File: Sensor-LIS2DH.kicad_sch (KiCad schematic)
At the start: 4 parts, among them U5 LIS2DH

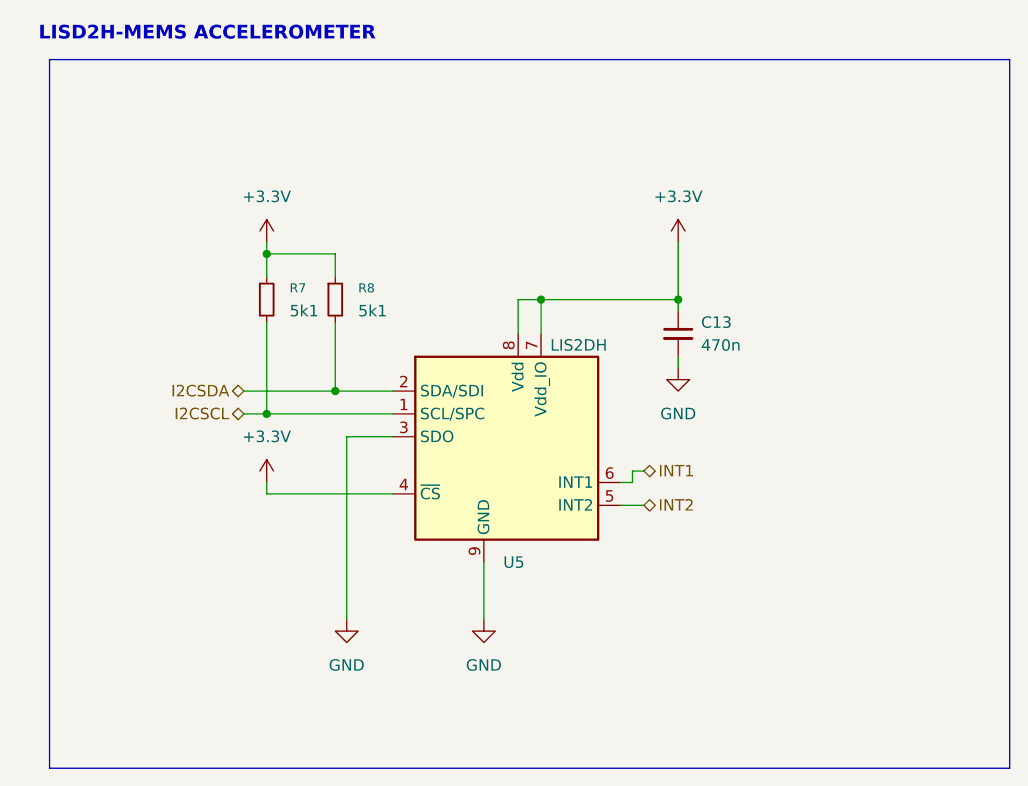
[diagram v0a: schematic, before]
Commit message: fix(hardware): update LIS2DH sensor schematic with corrected routing and metadata
- Adjust wire routing for INT1 signal path on Sensor-LIS2DH schematic
- Update datasheet URL to STMicroelectronics lis2dh12.pdf
- Add manufacturer, supplier, and part number metadata to component
- Add KLC compliance properties (KLC_S3.3, KLC_S4.1) to symbol and footprint entries
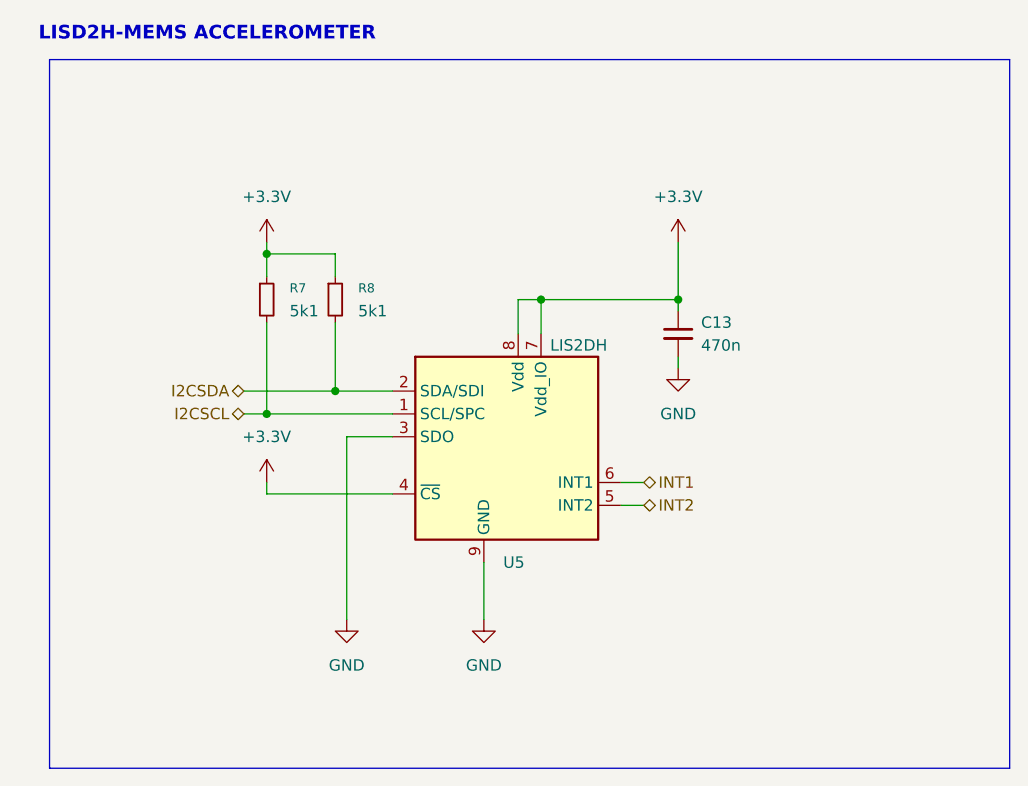
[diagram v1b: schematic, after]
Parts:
- U5: Distributor Link 1 (none) -> https://eu.mouser.com/ProductDetail/STMicroelectronics/LIS2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; Distributor Link 2  (none) -> https://www.digikey.com/en/products/detail/stmicroelectroni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; LCSC (none) -> C110926; Manufacturer (none) -> STMicroelectronics; Manufacturer part Number (none) -> LIS2DH12TR
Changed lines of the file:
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@@
-	(wire
-		(pts
-			(xy 88.9 76.2) (xy 88.9 77.47)
-		)
-		(stroke
-			(width 0)
-			(type default)
-		)
-	)
 	(wire
 		(pts
@@
 	(wire
 		(pts
-			(xy 88.9 77.47) (xy 87.63 77.47)
+			(xy 87.63 77.47) (xy 90.17 77.47)
 		)
 		(stroke
@@
 		(pts
 			(xy 48.26 77.47) (xy 48.26 78.74)
-		)
-		(stroke
-			(width 0)
-			(type default)
-		)
-	)
-	(wire
-		(pts
-			(xy 90.17 76.2) (xy 88.9 76.2)
 		)
 		(stroke
@@
 	(hierarchical_label "INT1"
 		(shape tri_state)
-		(at 90.17 76.2 0)
+		(at 90.17 77.47 0)
 		(effects
 			(font
@@
 			)
 		)
-		(property "Datasheet" "http://www.st.com/web/en/resource/technical/document/datasheet/DM00042751.pdf"
+		(property "Datasheet" "https://www.st.com/resource/en/datasheet/lis2dh12.pdf"
 			(at 72.39 88.9 0)
 			(effects
@@
 			)
 		)
-		(property "Description" "3-Axis Accelerometer, 2/4/8/16g range, I2C/SPI interface, LGA-14"
+		(property "Description" "Accelerometers MEMS digital output motion sensor: ultra-low-power high-performance 3-axis &#34;"
+			(at 72.39 73.66 0)
+			(effects
+				(font
+					(size 1.27 1.27)
+				)
+				(hide yes)
+			)
+		)
+		(property "Manufacturer" "STMicroelectronics"
+			(at 72.39 73.66 0)
+			(effects
+				(font
+					(size 1.27 1.27)
+				)
+				(hide yes)
+			)
+		)
+		(property "Manufacturer part Number" "LIS2DH12TR"
+			(at 72.39 73.66 0)
+			(effects
+				(font
+					(size 1.27 1.27)
+				)
+				(hide yes)
+			)
+		)
+		(property "Distributor Link 1" "https://eu.mouser.com/ProductDetail/STMicroelectronics/LIS2DH12TR?qs=yXzv9R%2FF42K6DbawEx3XmQ%3D%3D"
+			(at 72.39 73.66 0)
+			(effects
+				(font
+					(size 1.27 1.27)
+				)
+				(hide yes)
+			)
+		)
+		(property "Distributor Link 2 " "https://www.digikey.com/en/products/detail/stmicroelectronics/LIS2DH12TR/4899892?s=N4IgTCBcDaIDIEkDKYAiAJAjGAKgJRAF0BfIA"
+			(at 72.39 73.66 0)
+			(effects
+				(font
+					(size 1.27 1.27)
+				)
+				(hide yes)
+			)
+		)
+		(property "LCSC" "C110926"
+			(at 72.39 73.66 0)
+			(effects
+				(font
+					(size 1.27 1.27)
+				)
+				(hide yes)
+			)
+		)
+		(property "KLC_S3.3" ""
+			(at 72.39 73.66 0)
+			(effects
+				(font
+					(size 1.27 1.27)
+				)
+				(hide yes)
+			)
+		)
+		(property "KLC_S4.1" ""
 			(at 72.39 73.66 0)
 			(effects
@@
 			)
 		)
+		(property "KLC_S3.3" ""
+			(at 48.26 57.15 0)
+			(effects
+				(font
+					(size 1.27 1.27)
+				)
+				(hide yes)
+			)
+		)
+		(property "KLC_S4.1" ""
+			(at 48.26 57.15 0)
+			(effects
+				(font
+					(size 1.27 1.27)
+				)
+				(hide yes)
+			)
+		)
 		(pin "1"
 		)
@@
 			)
 		)
+		(property "KLC_S3.3" ""
+			(at 55.88 57.15 0)
+			(effects
+				(font
+					(size 1.27 1.27)
+				)
+				(hide yes)
+			)
+		)
+		(property "KLC_S4.1" ""
+			(at 55.88 57.15 0)
+			(effects
+				(font
+					(size 1.27 1.27)
+				)
+				(hide yes)
+			)
+		)
 		(pin "1"
 		)
@@
 			(at 93.98 60.96 0)
 			(effects
+				(font
+					(size 1.27 1.27)
+				)
+				(hide yes)
+			)
+		)
+		(property "KLC_S3.3" ""
+			(at 93.98 60.96 0)
+			(effects
+				(font
+					(size 1.27 1.27)
+				)
+				(hide yes)
+			)
+		)
+		(property "KLC_S4.1" ""
+			(at 93.98 60.96 0)
+			(effects

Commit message: fix(hardware): rearrange LIS2DH schematic hierarchical labels
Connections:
- net INT1: now also U5.5 (INT2); no longer U5.6 (INT1)
- net INT2: no longer U5.5 (INT2)
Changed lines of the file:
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@@
+		)
+	)
+	(hierarchical_label "INT1"
+		(shape tri_state)
+		(at 90.17 80.01 0)
+		(effects
+			(font
+				(size 1.27 1.27)
+			)
+			(justify left)
+		)
+	)
+	(hierarchical_label "INT2"
+		(shape tri_state)
+		(at 99.06 85.09 0)
+		(effects
+			(font
+				(size 1.27 1.27)
+			)
+			(justify left)
 		)
 	)
@@
 		)
 	)
-	(hierarchical_label "INT1"
-		(shape tri_state)
-		(at 90.17 77.47 0)
-		(effects
-			(font
-				(size 1.27 1.27)
-			)
-			(justify left)
-		)
-	)
 	(hierarchical_label "I2CSCL"
 		(shape tri_state)
@@
 		)
 	)
-	(hierarchical_label "INT2"
-		(shape tri_state)
-		(at 90.17 80.01 0)
-		(effects
-			(font
-				(size 1.27 1.27)
-			)
-			(justify left)
-		)
-	)

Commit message: fix(hardware): reposition INT2 hierarchical label in LIS2DH schematic
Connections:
- net INT2: now also U5.6 (INT1)
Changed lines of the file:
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@@
 	(hierarchical_label "INT2"
 		(shape tri_state)
-		(at 99.06 85.09 0)
+		(at 90.17 77.47 0)
 		(effects
 			(font
